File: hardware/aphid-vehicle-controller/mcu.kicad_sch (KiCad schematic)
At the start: 18 parts, among them J3 MAIN_DEBUG, J4 SWD, U1 STM32G491CETx, Y1 8 MHz

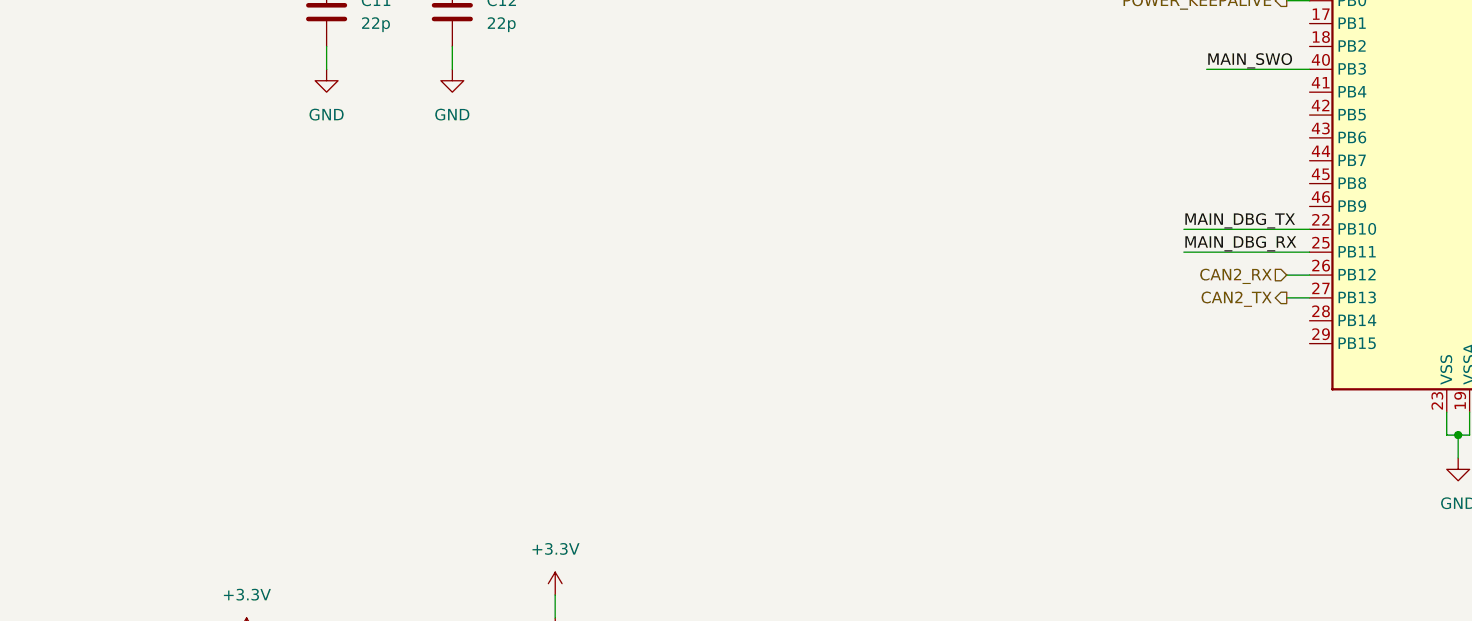
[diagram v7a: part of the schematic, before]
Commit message: Harmonized VC and BMS components
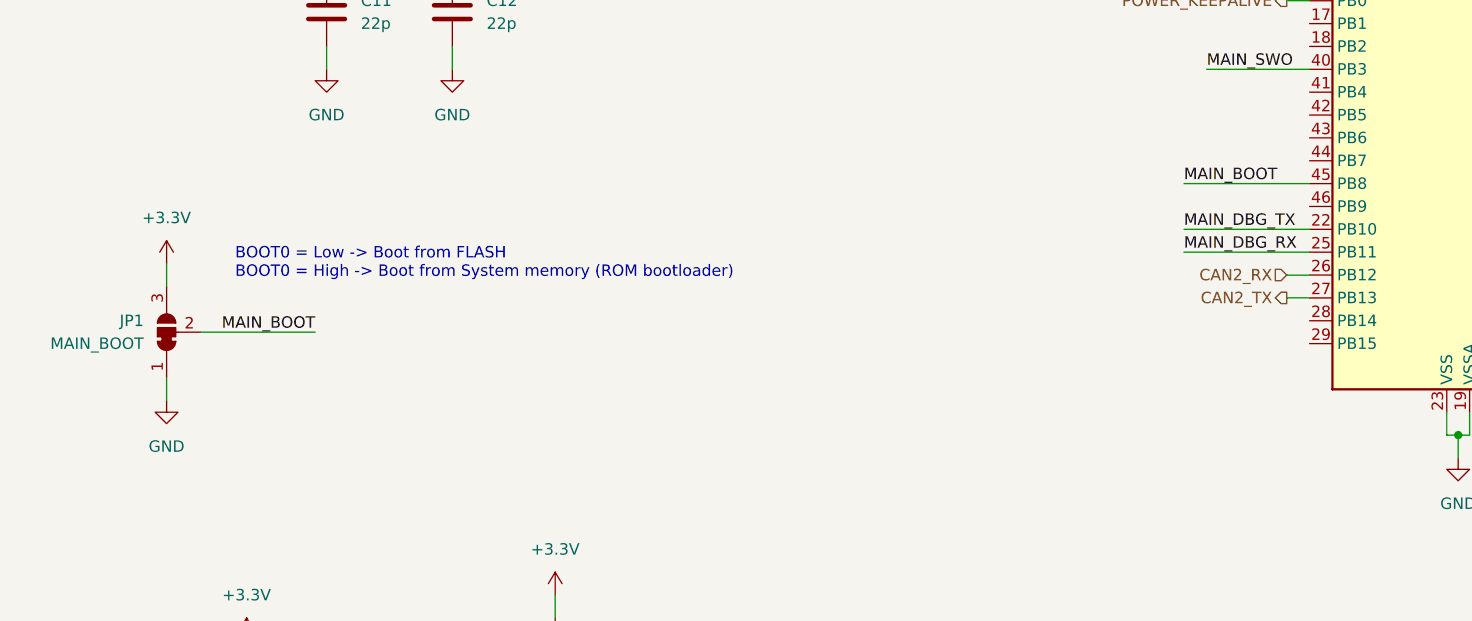
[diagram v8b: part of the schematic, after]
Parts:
- added JP1: MAIN_BOOT, symbol Jumper:SolderJumper_3_Bridged12
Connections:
- net +3.3V: now also JP1.3 (B)
- net GND: now also JP1.1 (A)
- net MAIN_BOOT: now reaches U1.45 (PB8)
- net MAIN_BOOT: now also JP1.2 (C)
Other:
- note added: "BOOT0 = Low -> Boot from FLASH BOOT0 = High -> Boot from System memory (ROM bootloader)"
